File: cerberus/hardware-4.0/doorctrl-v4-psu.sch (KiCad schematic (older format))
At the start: 34 parts, among them U2 MC34063, U3 L4960

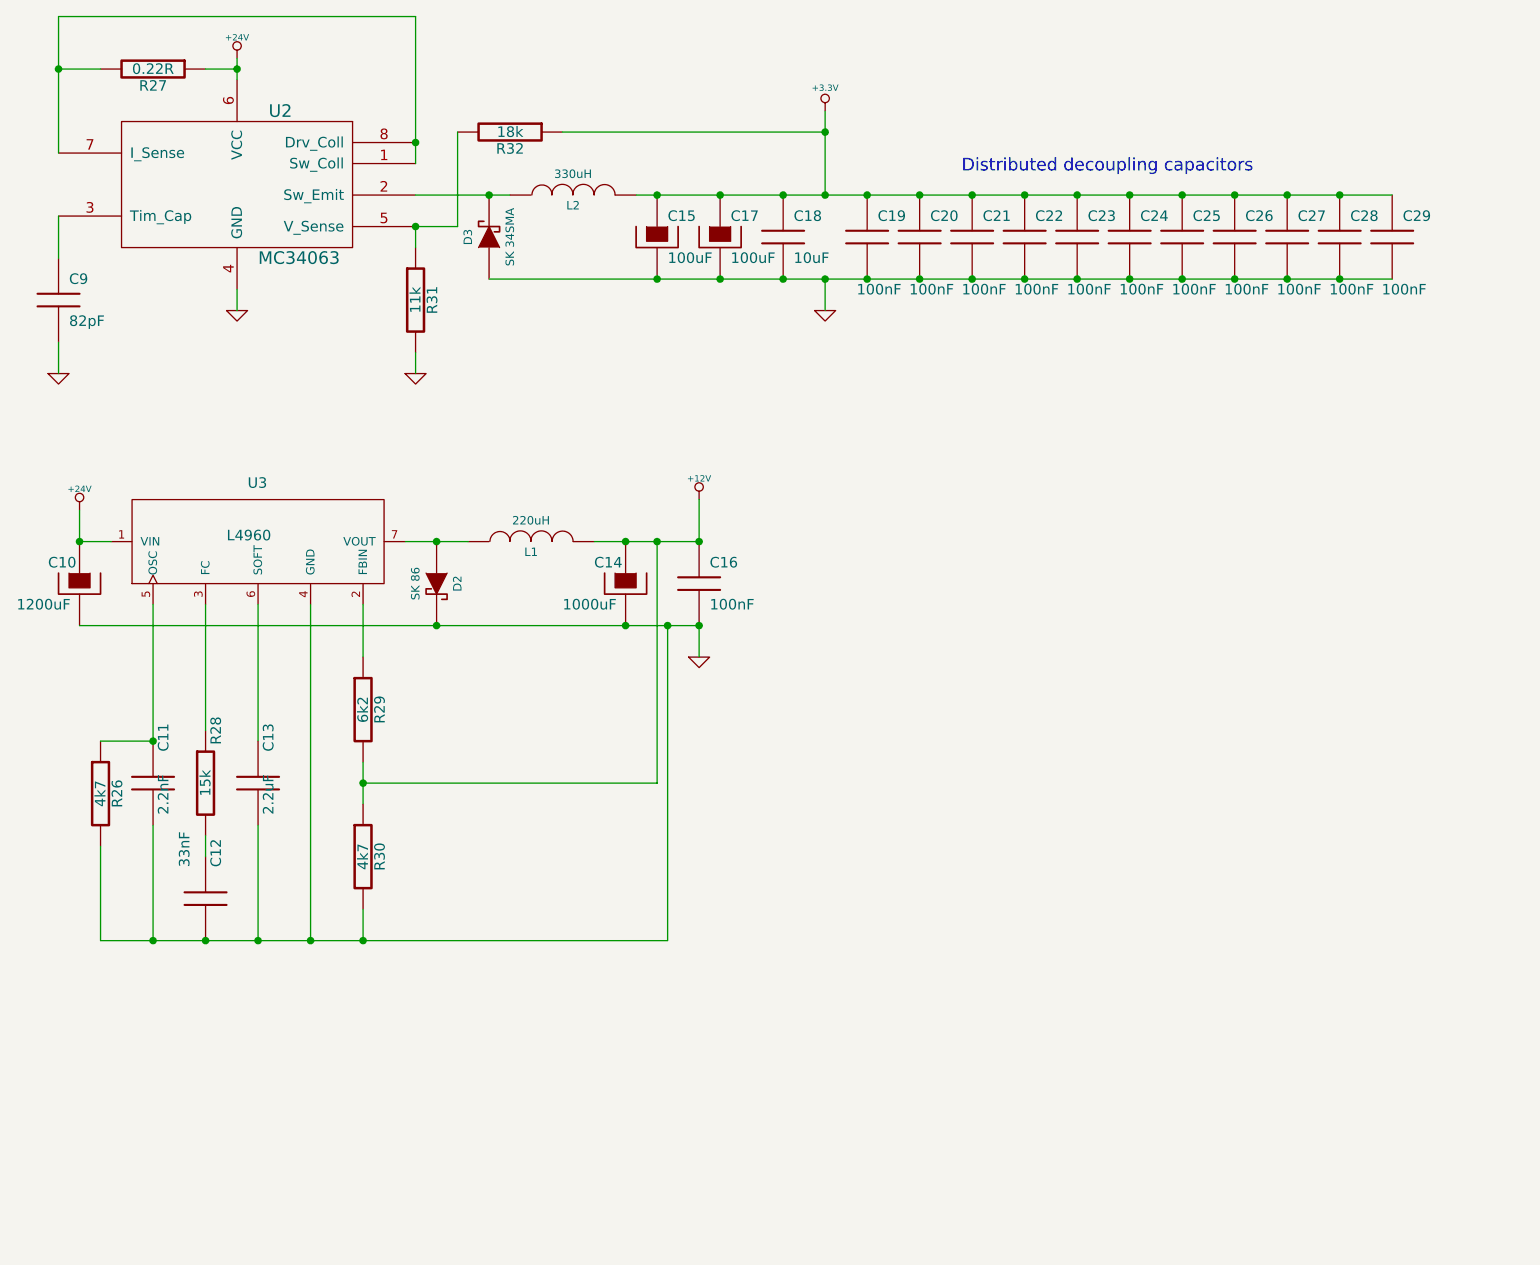
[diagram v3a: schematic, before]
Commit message: Added a 5V regulator for most stuff, except ENC28J60 which lives on its own 3.3v supply
git-svn-id: file:///home/ff/projects/osaa/svn@217 a092026d-3e22-4cff-94a7-eaa6fdd35d37
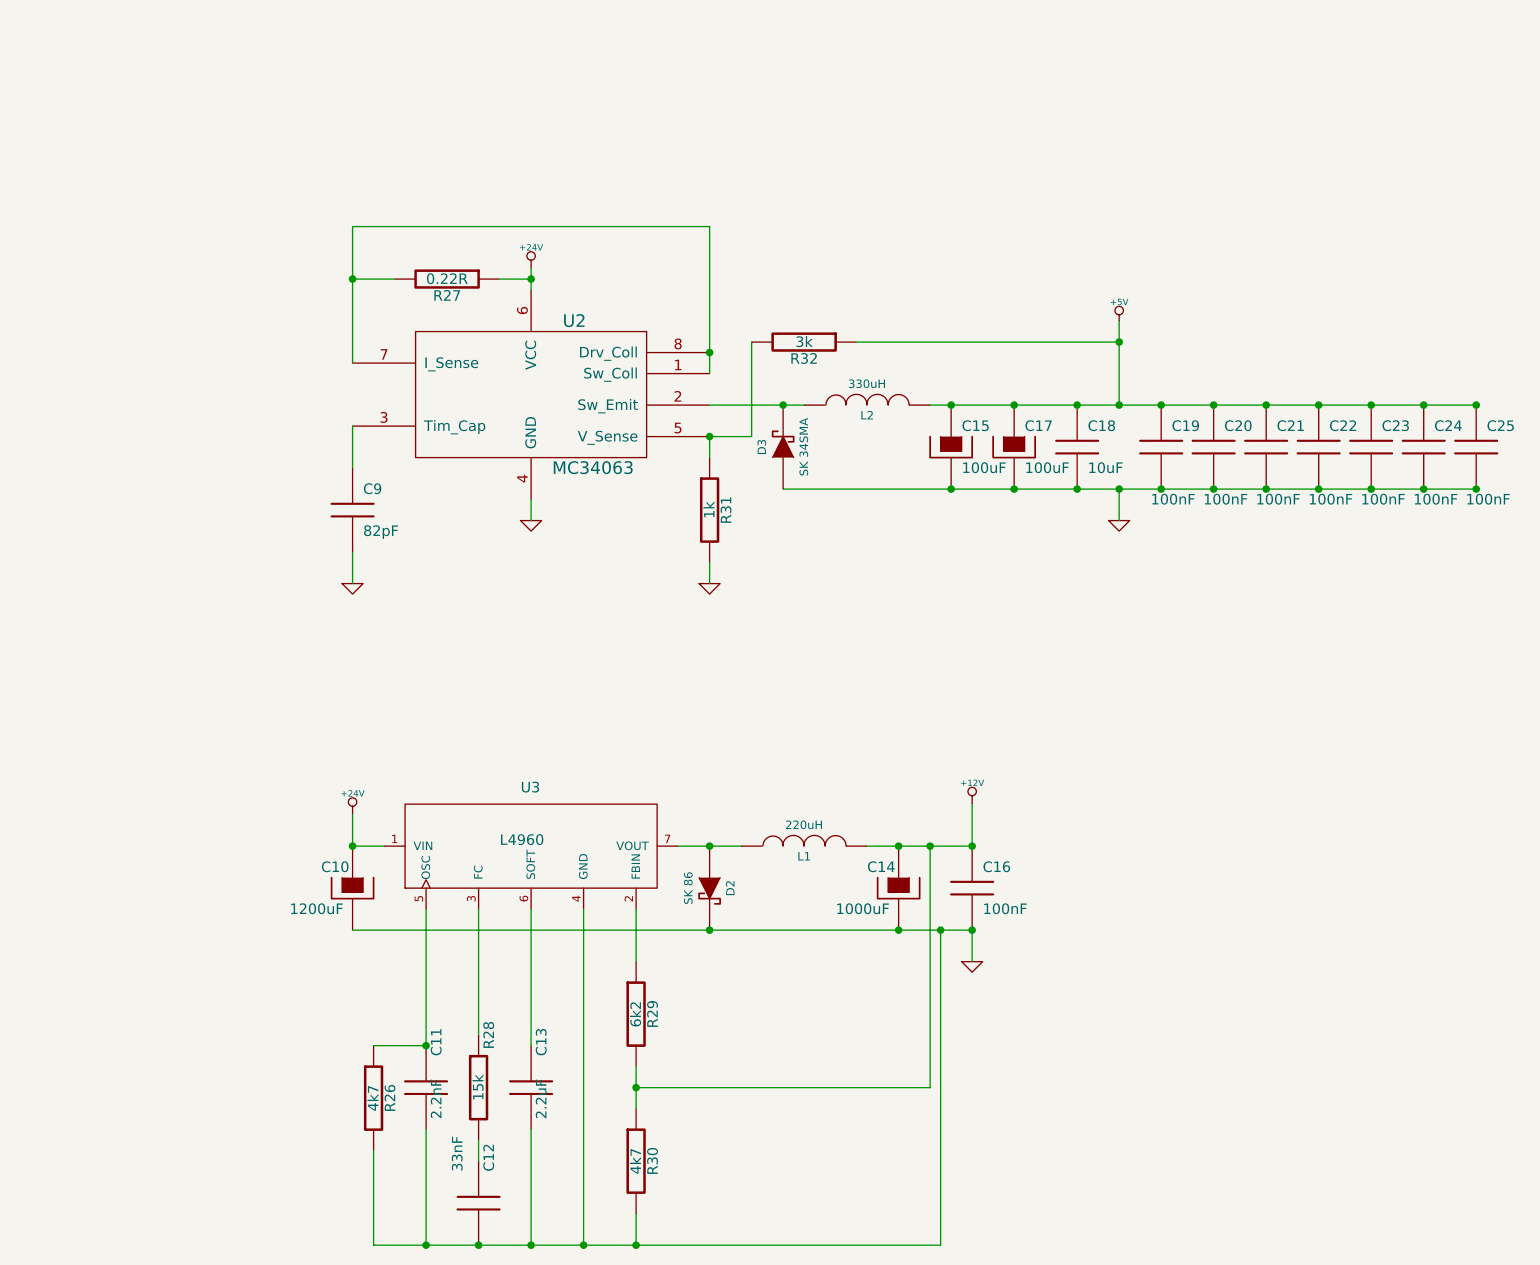
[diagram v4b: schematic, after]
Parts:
- removed C26, C27, C28, C29: 100nF, symbol C
- R31: value 11k -> 1k
- R32: value 18k -> 3k
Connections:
- net +3.3V renamed +5V
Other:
- note removed: "Distributed decoupling capacitors"
- moved on the sheet: C10, C11, C12, C13, C14, C15, C16, C17, C18, C19, C20, C21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
